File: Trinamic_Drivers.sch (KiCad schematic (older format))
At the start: 60 parts, among them J10 CHECK FOOTPRINT, J11 Conn_01x02_Male, J6 CHECK FOOTPRINT, J7 CHECK FOOTPRINT, J8 Conn_01x02_Male, J9 Conn_01x02_Male, U6 TMC2130-LA, U7 TMC2130-LA, U8 TMC2130-LA

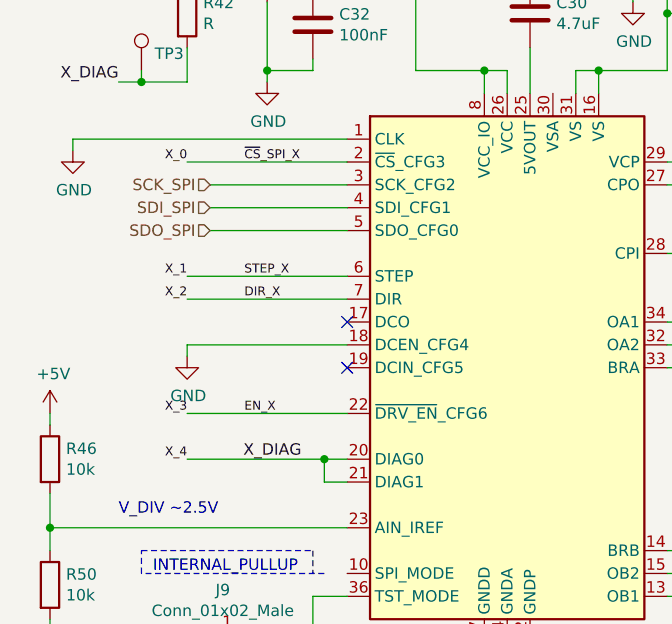
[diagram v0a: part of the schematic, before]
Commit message: Fixed X,Y,Z driver bus connection. set up spare and X2
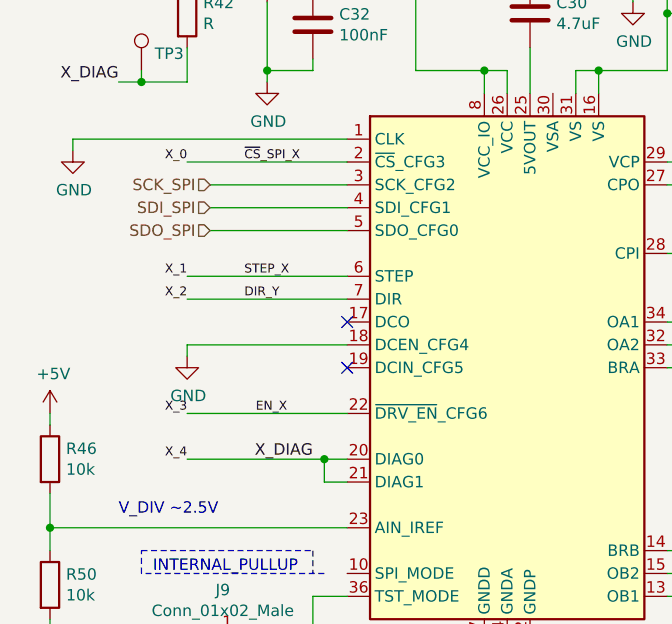
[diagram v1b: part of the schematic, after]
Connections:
- net DIR_X is gone; now on net DIR_Y: U7.7 (DIR)
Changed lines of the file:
@@
 Text Label 5900 2800 0    39   ~ 0
 EN_Y
-Text Label 1750 3050 2    50   ~ 0
-X_DIAG
 Connection ~ 1850 3050
 Wire Wire Line
@@
 Wire Wire Line
 	1950 1950 1350 1950
-Wire Wire Line
-	1950 1850 1350 1850
 Text HLabel 1350 2050 0    50   Input ~ 0
 SDO_SPI
 Text HLabel 1350 1950 0    50   Input ~ 0
 SDI_SPI
-Text HLabel 1350 1850 0    50   Input ~ 0
-SCK_SPI
 $Comp
 L power:GND #PWR?
@@
 Text Label 1300 5700 2    39   ~ 0
 SDO_SPI
-Text Label 1500 1750 0    39   ~ 0
-~CS~_SPI_X
-Text Label 1500 2250 0    39   ~ 0
-STEP_X
-Text Label 1500 2350 0    39   ~ 0
-DIR_X
-Text Label 1500 2850 0    39   ~ 0
-EN_X
 Wire Wire Line
 	4550 7050 4700 7050
@@
 Text Label 1250 3050 2    39   ~ 0
 X_4
-Wire Wire Line
-	1250 1750 1950 1750
 Wire Wire Line
 	1250 2250 1950 2250
@@
 Wire Wire Line
 	950  6500 1900 6500
+Wire Wire Line
+	1950 1750 1250 1750
+Text HLabel 1350 1850 0    50   Input ~ 0
+SCK_SPI
+Wire Wire Line
+	1950 1850 1350 1850
 Wire Bus Line
 	4800 6750 4800 7700
@@
 Wire Bus Line
 	6200 6750 6200 7700
+Text Label 1500 1750 0    39   ~ 0
+~CS~_SPI_X
+Text Label 1500 2250 0    39   ~ 0
+STEP_X
+Text Label 1500 2350 0    39   ~ 0
+DIR_Y
+Text Label 1550 2850 0    39   ~ 0
+EN_X
+Text Label 1800 3050 2    50   ~ 0
+X_DIAG
 $EndSCHEMATC

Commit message: updated ATMEGA and regulators
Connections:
- net +5V: now also C38.2, U6.30 (VSA), U7.30 (VSA), U8.25 (5VOUT), U8.30 (VSA)
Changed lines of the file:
@@
 Connection ~ 2250 1000
 Wire Wire Line
-	2250 1000 2250 1350
+	2250 1000 2250 1200
 Wire Wire Line
 	1800 1300 1800 1350
@@
 Connection ~ 6650 950
 Wire Wire Line
-	6650 950  6650 1300
+	6650 950  6650 1150
 Wire Wire Line
 	6200 1250 6200 1300
@@
 Connection ~ 2200 4650
 Wire Wire Line
-	2200 4650 2200 5000
+	2200 4650 2200 4900
 Wire Wire Line
 	1750 4950 1750 5000
@@
 Text Label 1800 3050 2    50   ~ 0
 X_DIAG
+Wire Wire Line
+	2850 1450 2850 1200
+Wire Wire Line
+	2850 1200 2250 1200
+Connection ~ 2250 1200
+Wire Wire Line
+	2250 1200 2250 1350
+Wire Wire Line
+	7250 1400 7250 1150
+Wire Wire Line
+	7250 1150 6650 1150
+Connection ~ 6650 1150
+Wire Wire Line
+	6650 1150 6650 1300
+Wire Wire Line
+	2800 5100 2800 4900
+Wire Wire Line
+	2800 4900 2700 4900
+Connection ~ 2200 4900
+Wire Wire Line
+	2200 4900 2200 5000
+Connection ~ 2700 4900
+Wire Wire Line
+	2700 4900 2200 4900
 Wire Bus Line
 	4800 6750 4800 7700

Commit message: added footprints for most of the c,r, and tp's. need new buck
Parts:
- R39, R40, R51: footprint (none) -> Resistors_SMD:R_0603_HandSoldering
- TP2, TP3, TP4: footprint Measurement_Points:Test_Point_Keystone_5000-5004_Miniature -> Measurement_Points:Test_Point_Keystone_5015_Micro-Minature
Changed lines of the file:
@@
 EESchema Schematic File Version 4
-EELAYER 30 0
+LIBS:bountifulHarvest-cache
+EELAYER 26 0
 EELAYER END
 $Descr A4 11693 8268
@@
 F 0 "TP3" H 1108 1424 50  0000 L CNN
 F 1 "TestPoint" H 1108 1379 50  0001 L CNN
-F 2 "Measurement_Points:Test_Point_Keystone_5000-5004_Miniature" H 1250 1350 50  0001 C CNN
+F 2 "Measurement_Points:Test_Point_Keystone_5015_Micro-Minature" H 1250 1350 50  0001 C CNN
 F 3 "~" H 1250 1350 50  0001 C CNN
 	1    1050 1350
@@
 F 0 "R40" V 2293 900 50  0000 C CNN
 F 1 "10" V 2384 900 50  0000 C CNN
-F 2 "" V 2430 900 50  0001 C CNN
+F 2 "Resistors_SMD:R_0603_HandSoldering" V 2430 900 50  0001 C CNN
 F 3 "~" H 2500 900 50  0001 C CNN
 F 4 "Digi-Key" H 2500 900 50  0001 C CNN "Vendor"
@@
 F 0 "TP2" H 5508 1374 50  0000 L CNN
 F 1 "TestPoint" H 5508 1329 50  0001 L CNN
-F 2 "Measurement_Points:Test_Point_Keystone_5000-5004_Miniature" H 5650 1300 50  0001 C CNN
+F 2 "Measurement_Points:Test_Point_Keystone_5015_Micro-Minature" H 5650 1300 50  0001 C CNN
 F 3 "~" H 5650 1300 50  0001 C CNN
 	1    5450 1300
@@
 F 0 "R39" V 6693 850 50  0000 C CNN
 F 1 "10" V 6784 850 50  0000 C CNN
-F 2 "" V 6830 850 50  0001 C CNN
+F 2 "Resistors_SMD:R_0603_HandSoldering" V 6830 850 50  0001 C CNN
 F 3 "~" H 6900 850 50  0001 C CNN
 F 4 "Digi-Key" H 6900 850 50  0001 C CNN "Vendor"
@@
 F 0 "TP4" H 1058 5074 50  0000 L CNN
 F 1 "TestPoint" H 1058 5029 50  0001 L CNN
-F 2 "Measurement_Points:Test_Point_Keystone_5000-5004_Miniature" H 1200 5000 50  0001 C CNN
+F 2 "Measurement_Points:Test_Point_Keystone_5015_Micro-Minature" H 1200 5000 50  0001 C CNN
 F 3 "~" H 1200 5000 50  0001 C CNN
 	1    1000 5000
@@
 F 0 "R51" V 2243 4550 50  0000 C CNN
 F 1 "10" V 2334 4550 50  0000 C CNN
-F 2 "" V 2380 4550 50  0001 C CNN
+F 2 "Resistors_SMD:R_0603_HandSoldering" V 2380 4550 50  0001 C CNN
 F 3 "~" H 2450 4550 50  0001 C CNN
 F 4 "Digi-Key" H 2450 4550 50  0001 C CNN "Vendor"
